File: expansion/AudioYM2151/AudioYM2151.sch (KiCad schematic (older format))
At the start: 3 parts

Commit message: Added YM2151 amp to seperate sheet
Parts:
- removed U?: SN74AVC8T245PW, Package_SO:TSSOP-24_4.4x7.8mm_P0.65mm, symbol Logic_LevelTranslator:SN74AVC8T245PW
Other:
- moved on the sheet: J?, U?
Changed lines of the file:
@@
 $Descr A3 16535 11693
 encoding utf-8
-Sheet 1 2
+Sheet 1 4
 Title ""
 Date ""
@@
 L CPLD_Xilinx:XC95144XL-TQ100 U?
 U 1 1 60B018A5
-P 8900 4200
-F 0 "U?" H 8900 7081 50  0000 C CNN
-F 1 "XC95144XL-TQ100" H 8900 6990 50  0000 C CNN
-F 2 "Package_QFP:TQFP-100_14x14mm_P0.5mm" H 8900 4200 50  0001 C CNN
-F 3 "https://www.xilinx.com/support/documentation/data_sheets/ds056.pdf" H 8900 4200 50  0001 C CNN
-	1    8900 4200
+P 7100 3750
+F 0 "U?" H 7100 6631 50  0000 C CNN
+F 1 "XC95144XL-TQ100" H 7100 6540 50  0000 C CNN
+F 2 "Package_QFP:TQFP-100_14x14mm_P0.5mm" H 7100 3750 50  0001 C CNN
+F 3 "https://www.xilinx.com/support/documentation/data_sheets/ds056.pdf" H 7100 3750 50  0001 C CNN
+	1    7100 3750
 	1    0    0    -1
 $EndComp
@@
 L Ddraig:D68K_64PIN_BOARD J?
 U 1 1 60B07460
-P 2950 4000
-F 0 "J?" H 2925 6065 50  0000 C CNN
-F 1 "D68K_64PIN_BOARD" H 2925 5974 50  0000 C CNN
-F 2 "Ddraig:DIN41612_C_2x32_Male_Horizontal_THT" H 2800 2750 50  0001 C CNN
-F 3 "" H 2800 2750 50  0001 C CNN
-	1    2950 4000
+P 2900 3500
+F 0 "J?" H 2875 5565 50  0000 C CNN
+F 1 "D68K_64PIN_BOARD" H 2875 5474 50  0000 C CNN
+F 2 "Ddraig:DIN41612_C_2x32_Male_Horizontal_THT" H 2750 2250 50  0001 C CNN
+F 3 "" H 2750 2250 50  0001 C CNN
+	1    2900 3500
 	1    0    0    -1
 $EndComp
 $Sheet
-S 11900 3250 1850 2000
+S 10300 5700 1850 1550
 U 60B0BE0A
-F0 "Audio" 50
-F1 "Audio.sch" 50
+F0 "YM2151" 50
+F1 "YM2151.sch" 50
+F2 "A1" I L 10300 6000 50
+F3 "~CS_YM" I L 10300 6100 50
+F4 "~RD_YM" I L 10300 6200 50
+F5 "~WR_YM" I L 10300 6300 50
+F6 "~RESET" I L 10300 6400 50
+F7 "~IRQ" I L 10300 6500 50
+F8 "SPI_DI" I L 10300 6650 50
+F9 "SPI_CLK" I L 10300 6750 50
+F10 "SPI_YMCLK" I L 10300 6850 50
+F11 "YM_AUDIO_L" O R 12150 6050 50
+F12 "YM_AUDIO_R" O R 12150 6150 50
 $EndSheet
-$Comp
-L Logic_LevelTranslator:SN74AVC8T245PW U?
-U 1 1 60B052FD
-P 6350 3950
-F 0 "U?" H 6350 3161 50  0000 C CNN
-F 1 "SN74AVC8T245PW" H 6350 3070 50  0000 C CNN
-F 2 "Package_SO:TSSOP-24_4.4x7.8mm_P0.65mm" H 7250 3300 50  0001 C CNN
-F 3 "https://www.ti.com/lit/ds/symlink/sn74avc8t245.pdf" H 6300 3700 50  0001 C CNN
-	1    6350 3950
-	1    0    0    -1
-$EndComp
+$Sheet
+S 13350 4300 1350 1250
+U 60CBD7B5
+F0 "Amplifier" 50
+F1 "Amplifier.sch" 50
+$EndSheet
+$Sheet
+S 10450 2700 1800 1400
+U 60D530A5
+F0 "ADPCM" 50
+F1 "ADPCM.sch" 50
+$EndSheet
 $EndSCHEMATC

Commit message: More work on YM2151
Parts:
- removed U?: XC95144XL-TQ100, Package_QFP:TQFP-100_14x14mm_P0.5mm, symbol CPLD_Xilinx:XC95144XL-TQ100
- added C? (x3): 100nF, symbol Device:C
- added D?: LED, symbol Device:LED
- added R?: 10K, symbol Device:R
- added R?: 150R, symbol Device:R
- added U?: XC95144XL-TQ100, Package_QFP:TQFP-100_14x14mm_P0.5mm, symbol CPLD_Xilinx:XC95144XL-TQ100
- added U? (x5): 74LS125, symbol 74xx:74LS125
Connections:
- net +5V: now reaches J?.A1 (+5V)
- net +5V: now also J?.A24 (+5V), J?.C1 (+5V), C?.1, C?.1, C?.1, U?.10, U?.12, U?.13, U?.14 (VCC), U?.9
- net D14: now reaches J?.A10 (D14)
- net D14: now also U?.79 (P79)
- net GND: now reaches J?.A11 (GND)
- net GND: now also J?.A2 (GND), J?.A32 (GND), J?.C11 (GND), J?.C24 (GND), J?.C29 (~PRD), J?.C32 (GND), C?.2, C?.2, C?.2, D?.1 (K), R?.2, U?.100 (GND), U?.2, U?.21 (GND), U?.31 (GND), U?.44 (GND), U?.5, U?.62 (GND), U?.69 (GND), U?.7 (GND), U?.75 (GND), U?.84 (GND)
- net A1: now reaches J?.A12 (A1)
- net A1: now also U?.11 (P11)
- net A3: now reaches J?.A13 (A3)
- net A3: now also U?.13 (P13)
- net A5: now reaches J?.A14 (A5)
- net A5: now also U?.15 (P15)
- net A7: now reaches J?.A15 (A7)
- net A7: now also U?.17 (P17)
- net ~LDS: now reaches J?.A25 (~LDS)
- net R~W: now reaches J?.A26 (R/~W)
- net CS_REG: now reaches J?.A27 (~ID)
- net at J?.A28 (~IRQ): now also U?.3
- net D0: now reaches J?.A3 (D0)
- net D0: now also U?.35 (P35)
- net +12V: now reaches J?.A31 (+12V)
- net +12V: now also J?.C31 (+12V)
- net D2: now reaches J?.A4 (D2)
- net D2: now also U?.37 (P37)
- net D4: now reaches J?.A5 (D4)
- net D4: now also U?.40 (P40)
- net D6: now reaches J?.A6 (D6)
- net D6: now also U?.42 (P42)
- net D8: now reaches J?.A7 (D8)
- net D8: now also U?.46 (P46)
- net D10: now reaches J?.A8 (D10)
- net D10: now also U?.74 (P74)
- net D12: now reaches J?.A9 (D12)
- net D12: now also U?.77 (P77)
- net D15: now reaches J?.C10 (D15)
- net D15: now also U?.80 (P80)
- net A2: now reaches J?.C12 (A2)
- net A2: now also U?.12 (P12)
- net A4: now reaches J?.C13 (A4)
- net A4: now also U?.14 (P14)
- net A6: now reaches J?.C14 (A6)
- net A6: now also U?.16 (P16)
- net SYS_CLK: now reaches J?.C23 (SYS_CLK)
- net SYS_CLK: now also U?.22 (I/O/GCK1)
- net ~UDS: now reaches J?.C25 (~UDS)
- net ~RESET: now reaches J?.C26 (~RESET)
- net CS_DATA: now reaches J?.C27 (~CS)
- net at J?.C28 (~ACK): now also U?.6
- net D1: now reaches J?.C3 (D1)
- net D1: now also U?.36 (P36)
- net +3V3: now reaches J?.C30 (+3.3V)
- net +3V3: now also U?.26 (VCCIO), U?.38 (VCCIO), U?.5 (VCCINT), U?.51 (VCCIO), U?.57 (VCCINT), U?.88 (VCCIO), U?.98 (VCCINT)
- net D3: now reaches J?.C4 (D3)
- net D3: now also U?.39 (P39)
- net D5: now reaches J?.C5 (D5)
- net D5: now also U?.41 (P41)
- net D7: now reaches J?.C6 (D7)
- net D7: now also U?.43 (P43)
- net D9: now reaches J?.C7 (D9)
- net D9: now also U?.49 (P49)
- net D11: now reaches J?.C8 (D11)
- net D11: now also U?.76 (P76)
- net D13: now reaches J?.C9 (D13)
- net D13: now also U?.78 (P78)
- new net: D?.2 (A), R?.2
- new net LED: R?.1
- new net MCK: U?.23 (I/O/GCK2)
- new net SPI_DI: R?.1, U?.97 (P97)
- new net ~DTACK: U?.4
- new net ~IRQ: U?.1
- no-connect marks 0 -> 19
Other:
- moved on the sheet: J?

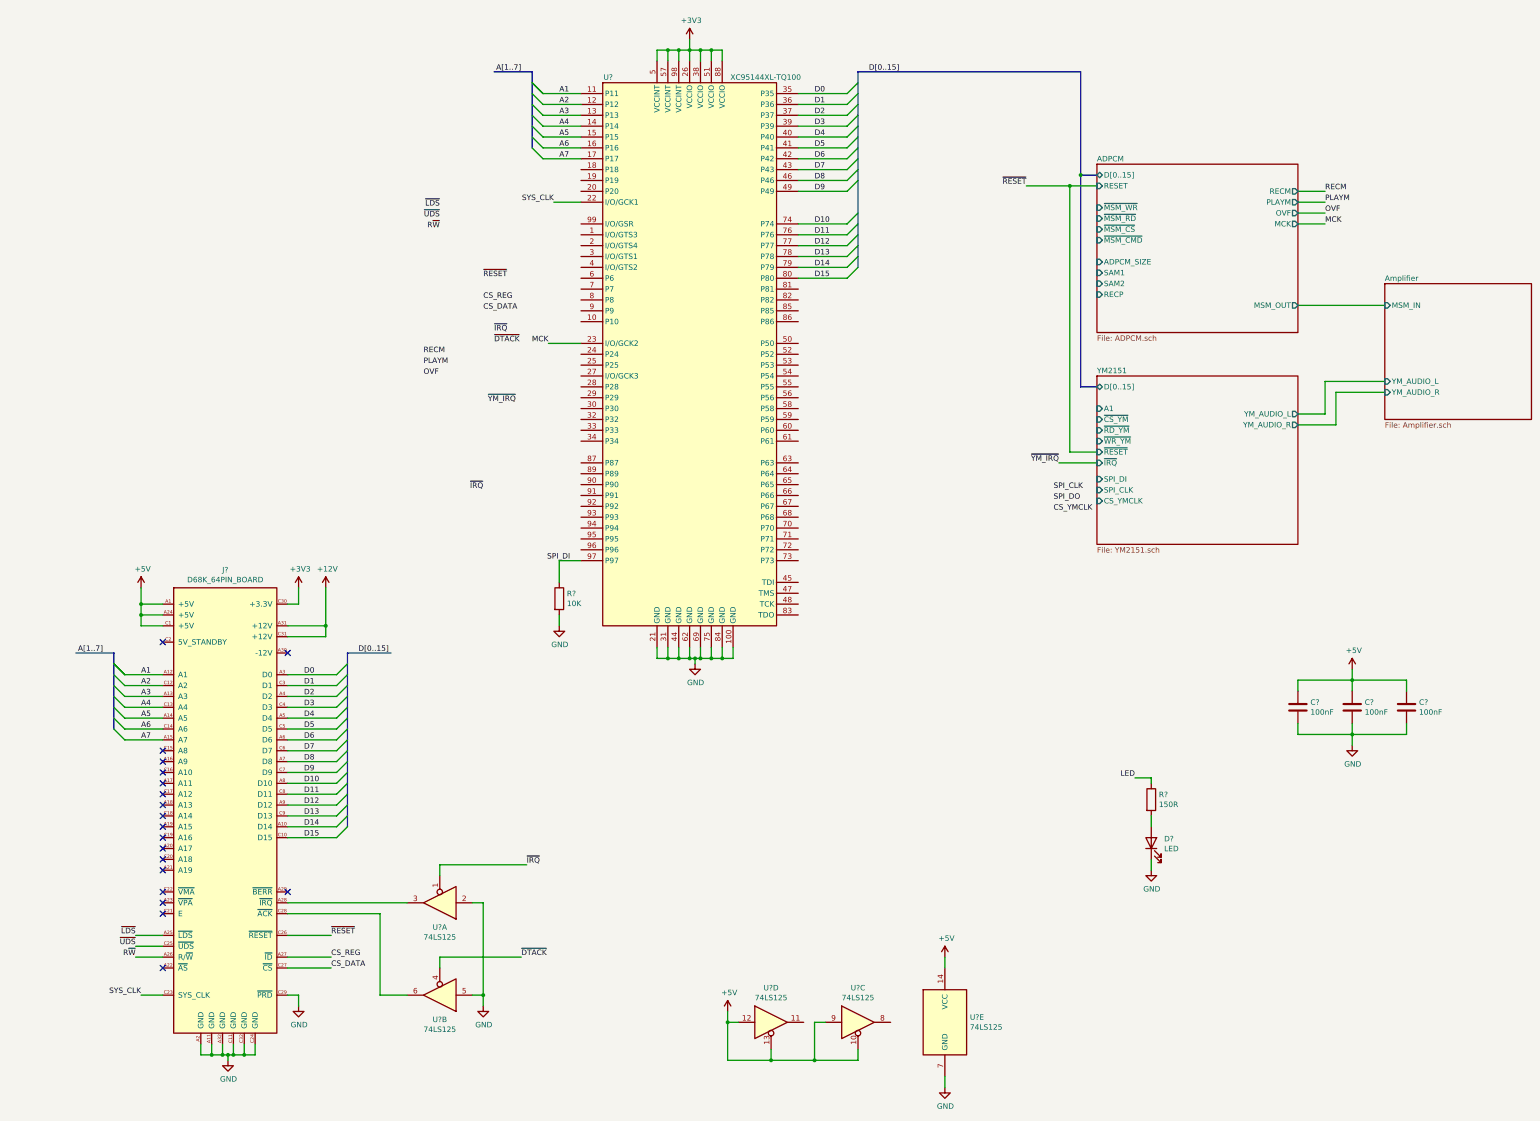
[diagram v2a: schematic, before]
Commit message: Started YM2151 board layout
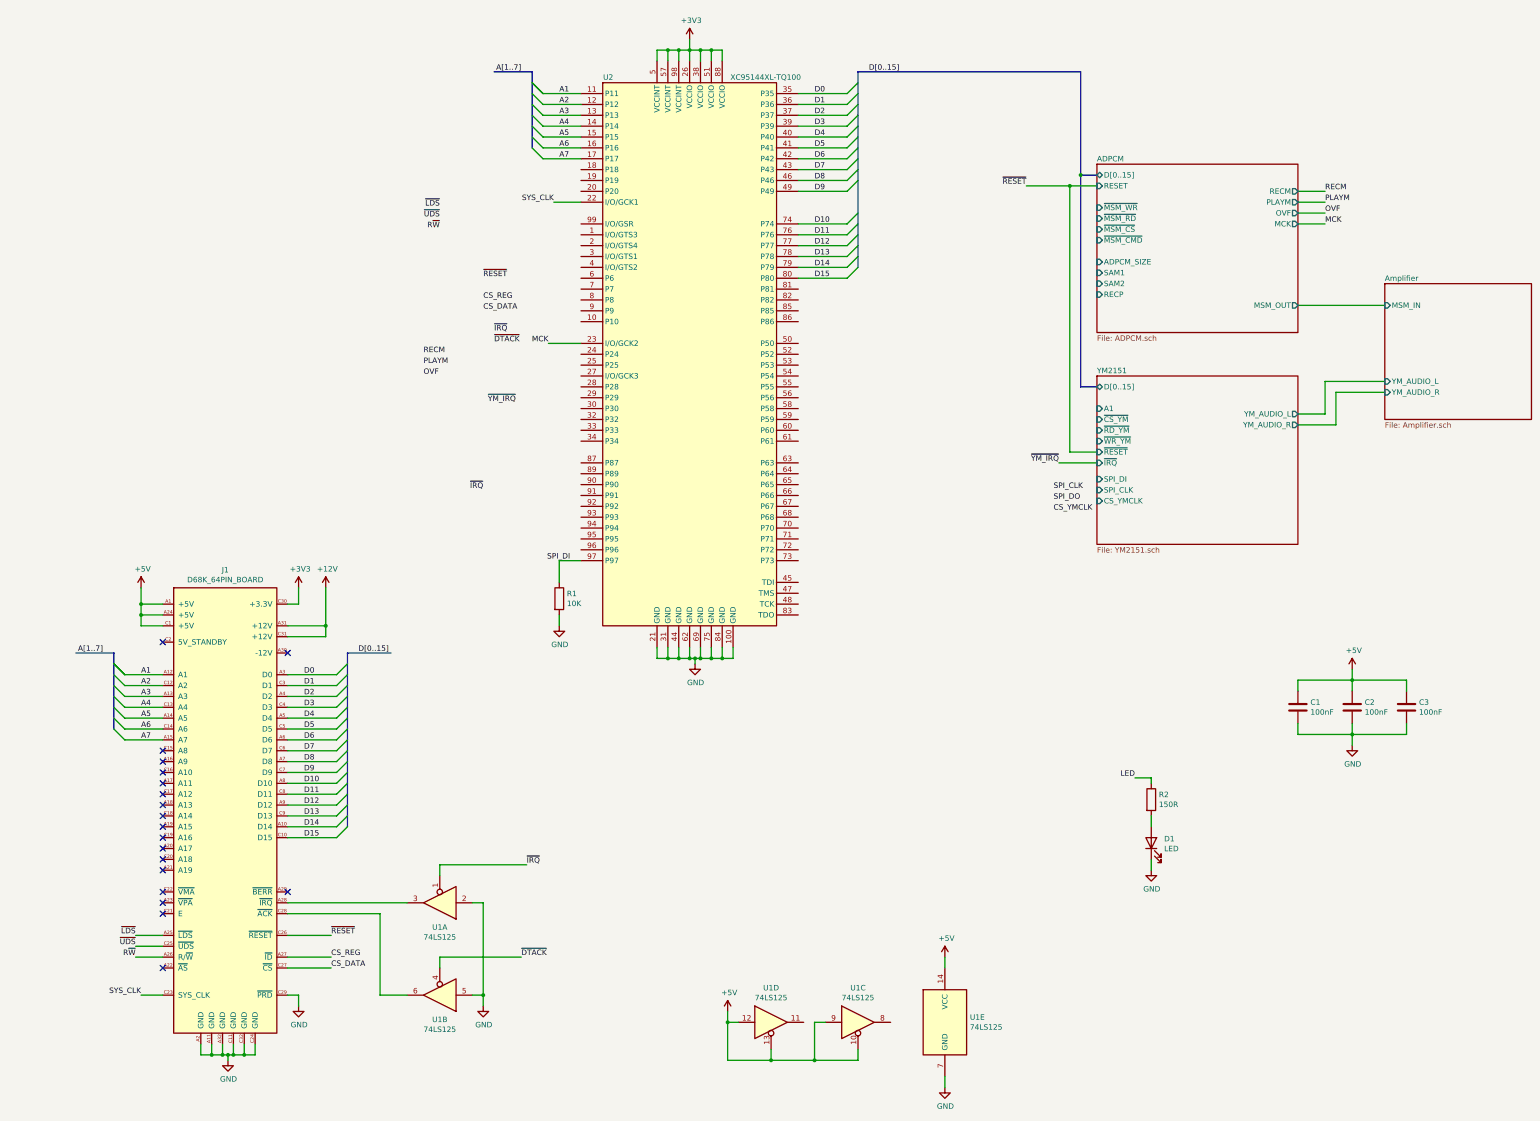
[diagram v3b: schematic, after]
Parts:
- C1, C2, C3: renamed from C?; footprint (none) -> Capacitor_THT:C_Disc_D5.0mm_W2.5mm_P2.50mm
- D1: renamed from D?; footprint (none) -> LED_THT:LED_D5.0mm
- R1, R2: renamed from R?; footprint (none) -> Resistor_THT:R_Axial_DIN0207_L6.3mm_D2.5mm_P10.16mm_Horizontal
- U1: renamed from U?; footprint (none) -> Package_DIP:DIP-14_W7.62mm_Socket
- gave numbers to parts that had none: 2
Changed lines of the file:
@@
 $EndDescr
 $Comp
-L Ddraig:D68K_64PIN_BOARD J?
+L Ddraig:D68K_64PIN_BOARD J1
 U 1 1 60B07460
 P 2850 8050
-F 0 "J?" H 2825 10115 50  0000 C CNN
+F 0 "J1" H 2825 10115 50  0000 C CNN
 F 1 "D68K_64PIN_BOARD" H 2825 10024 50  0000 C CNN
 F 2 "Ddraig:DIN41612_C_2x32_Male_Horizontal_THT" H 2700 6800 50  0001 C CNN
@@
 $EndSheet
 $Comp
-L CPLD_Xilinx:XC95144XL-TQ100 U?
+L CPLD_Xilinx:XC95144XL-TQ100 U2
 U 1 1 60CC8E00
 P 7100 4000
-F 0 "U?" H 6350 6550 50  0000 C CNN
+F 0 "U2" H 6350 6550 50  0000 C CNN
 F 1 "XC95144XL-TQ100" H 7800 6550 50  0000 C CNN
 F 2 "Package_QFP:TQFP-100_14x14mm_P0.5mm" H 7100 4000 50  0001 C CNN
@@
 NoConn ~ 3400 6750
 $Comp
-L power:+5V #PWR?
+L power:+5V #PWR0101
 U 1 1 60CD3C32
 P 2050 6150
-F 0 "#PWR?" H 2050 6000 50  0001 C CNN
+F 0 "#PWR0101" H 2050 6000 50  0001 C CNN
 F 1 "+5V" H 2065 6323 50  0000 C CNN
 F 2 "" H 2050 6150 50  0001 C CNN
@@
 $EndComp
 $Comp
-L power:+12V #PWR?
+L power:+12V #PWR0102
 U 1 1 60CD44DB
 P 3750 6150
-F 0 "#PWR?" H 3750 6000 50  0001 C CNN
+F 0 "#PWR0102" H 3750 6000 50  0001 C CNN
 F 1 "+12V" H 3765 6323 50  0000 C CNN
 F 2 "" H 3750 6150 50  0001 C CNN
@@
 NoConn ~ 3400 8950
 $Comp
-L power:GND #PWR?
+L power:GND #PWR0103
 U 1 1 60CE1A9B
 P 2850 10500
-F 0 "#PWR?" H 2850 10250 50  0001 C CNN
+F 0 "#PWR0103" H 2850 10250 50  0001 C CNN
 F 1 "GND" H 2855 10327 50  0000 C CNN
 F 2 "" H 2850 10500 50  0001 C CNN
@@
 $EndComp
 $Comp
-L power:GND #PWR?
+L power:GND #PWR0104
 U 1 1 60CE1DAE
 P 3500 10000
-F 0 "#PWR?" H 3500 9750 50  0001 C CNN
+F 0 "#PWR0104" H 3500 9750 50  0001 C CNN
 F 1 "GND" H 3505 9827 50  0000 C CNN
 F 2 "" H 3500 10000 50  0001 C CNN
@@
 	6100 2600 5850 2600
 $Comp
-L power:GND #PWR?
+L power:GND #PWR0105
 U 1 1 60CF6212
 P 7150 6850
-F 0 "#PWR?" H 7150 6600 50  0001 C CNN
+F 0 "#PWR0105" H 7150 6600 50  0001 C CNN
 F 1 "GND" H 7155 6677 50  0000 C CNN
 F 2 "" H 7150 6850 50  0001 C CNN
@@
 $EndComp
 $Comp
-L power:+3V3 #PWR?
+L power:+3V3 #PWR0106
 U 1 1 60CFD09B
 P 3500 6150
-F 0 "#PWR?" H 3500 6000 50  0001 C CNN
+F 0 "#PWR0106" H 3500 6000 50  0001 C CNN
 F 1 "+3V3" H 3515 6323 50  0000 C CNN
 F 2 "" H 3500 6150 50  0001 C CNN
@@
 	3500 6300 3500 6150
 $Comp
-L power:+3V3 #PWR?
+L power:+3V3 #PWR0107
 U 1 1 60CFFBD2
 P 7100 1100
-F 0 "#PWR?" H 7100 950 50  0001 C CNN
+F 0 "#PWR0107" H 7100 950 50  0001 C CNN
 F 1 "+3V3" H 7115 1273 50  0000 C CNN
 F 2 "" H 7100 1100 50  0001 C CNN
@@
 	7150 6800 7200 6800
 $Comp
-L 74xx:74LS125 U?
+L 74xx:74LS125 U1
 U 1 1 60F01C16
 P 4800 9050
-F 0 "U?" H 4800 9275 50  0000 C CNN
+F 0 "U1" H 4800 9275 50  0000 C CNN
 F 1 "74LS125" H 4800 9366 50  0000 C CNN
-F 2 "" H 4800 9050 50  0001 C CNN
+F 2 "Package_DIP:DIP-14_W7.62mm_Socket" H 4800 9050 50  0001 C CNN
 F 3 "http://www.ti.com/lit/gpn/sn74LS125" H 4800 9050 50  0001 C CNN
 	1    4800 9050
@@
 $EndComp
 $Comp
-L 74xx:74LS125 U?
+L 74xx:74LS125 U1
 U 2 1 60F033E0
 P 4800 9900
-F 0 "U?" H 4800 10125 50  0000 C CNN
+F 0 "U1" H 4800 10125 50  0000 C CNN
 F 1 "74LS125" H 4800 10216 50  0000 C CNN
-F 2 "" H 4800 9900 50  0001 C CNN
+F 2 "Package_DIP:DIP-14_W7.62mm_Socket" H 4800 9900 50  0001 C CNN
 F 3 "http://www.ti.com/lit/gpn/sn74LS125" H 4800 9900 50  0001 C CNN
 	2    4800 9900
@@
 $EndComp
 $Comp
-L 74xx:74LS125 U?
+L 74xx:74LS125 U1
 U 3 1 60F0459B
 P 8650 10150
-F 0 "U?" H 8650 10467 50  0000 C CNN
+F 0 "U1" H 8650 10467 50  0000 C CNN
 F 1 "74LS125" H 8650 10376 50  0000 C CNN
-F 2 "" H 8650 10150 50  0001 C CNN
+F 2 "Package_DIP:DIP-14_W7.62mm_Socket" H 8650 10150 50  0001 C CNN
 F 3 "http://www.ti.com/lit/gpn/sn74LS125" H 8650 10150 50  0001 C CNN
 	3    8650 10150
@@
 $EndComp
 $Comp
-L 74xx:74LS125 U?
+L 74xx:74LS125 U1
 U 4 1 60F05376
 P 7850 10150
-F 0 "U?" H 7850 10467 50  0000 C CNN
+F 0 "U1" H 7850 10467 50  0000 C CNN
 F 1 "74LS125" H 7850 10376 50  0000 C CNN
-F 2 "" H 7850 10150 50  0001 C CNN
+F 2 "Package_DIP:DIP-14_W7.62mm_Socket" H 7850 10150 50  0001 C CNN
 F 3 "http://www.ti.com/lit/gpn/sn74LS125" H 7850 10150 50  0001 C CNN
 	4    7850 10150
@@
 $EndComp
 $Comp
-L 74xx:74LS125 U?
+L 74xx:74LS125 U1
 U 5 1 60F0634B
 P 9450 10150
-F 0 "U?" H 9680 10196 50  0000 L CNN
+F 0 "U1" H 9680 10196 50  0000 L CNN
 F 1 "74LS125" H 9680 10105 50  0000 L CNN
-F 2 "" H 9450 10150 50  0001 C CNN
+F 2 "Package_DIP:DIP-14_W7.62mm_Socket" H 9450 10150 50  0001 C CNN
 F 3 "http://www.ti.com/lit/gpn/sn74LS125" H 9450 10150 50  0001 C CNN
 	5    9450 10150
@@
 	3400 9050 4500 9050
 $Comp
-L power:GND #PWR?
+L power:GND #PWR0108
 U 1 1 60F2C3F3
 P 5200 10000
-F 0 "#PWR?" H 5200 9750 50  0001 C CNN
+F 0 "#PWR0108" H 5200 9750 50  0001 C CNN
 F 1 "GND" H 5205 9827 50  0000 C CNN
 F 2 "" H 5200 10000 50  0001 C CNN
@@
 	4800 8700 5600 8700
 $Comp
-L power:GND #PWR?
+L power:GND #PWR0109
 U 1 1 60F41EEB
 P 9450 10750
-F 0 "#PWR?" H 9450 10500 50  0001 C CNN
+F 0 "#PWR0109" H 9450 10500 50  0001 C CNN
 F 1 "GND" H 9455 10577 50  0000 C CNN
 F 2 "" H 9450 10750 50  0001 C CNN
@@
 $EndComp
 $Comp
-L power:+5V #PWR?
+L power:+5V #PWR0110
 U 1 1 60F4243B
 P 9450 9550
-F 0 "#PWR?" H 9450 9400 50  0001 C CNN
+F 0 "#PWR0110" H 9450 9400 50  0001 C CNN
 F 1 "+5V" H 9465 9723 50  0000 C CNN
 F 2 "" H 9450 9550 50  0001 C CNN
@@
 	9450 10650 9450 10750
 $Comp
-L power:+5V #PWR?
+L power:+5V #PWR0111
 U 1 1 60F4D90B
 P 7450 10050
-F 0 "#PWR?" H 7450 9900 50  0001 C CNN
+F 0 "#PWR0111" H 7450 9900 50  0001 C CNN
 F 1 "+5V" H 7465 10223 50  0000 C CNN
 F 2 "" H 7450 10050 50  0001 C CNN
@@
 CS_YMCLK
 $Comp
-L Device:R R?
+L Device:R R1
 U 1 1 60FF10BA
 P 5900 6250
-F 0 "R?" H 5970 6296 50  0000 L CNN
+F 0 "R1" H 5970 6296 50  0000 L CNN
 F 1 "10K" H 5970 6205 50  0000 L CNN
-F 2 "" V 5830 6250 50  0001 C CNN
+F 2 "Resistor_THT:R_Axial_DIN0207_L6.3mm_D2.5mm_P10.16mm_Horizontal" V 5830 6250 50  0001 C CNN
 F 3 "~" H 5900 6250 50  0001 C CNN
 	1    5900 6250
@@
 $EndComp
 $Comp
-L power:GND #PWR?
+L power:GND #PWR0112
 U 1 1 60FF1314
 P 5900 6500
-F 0 "#PWR?" H 5900 6250 50  0001 C CNN
+F 0 "#PWR0112" H 5900 6250 50  0001 C CNN
 F 1 "GND" H 5905 6327 50  0000 C CNN
 F 2 "" H 5900 6500 50  0001 C CNN
@@
 SPI_DI
 $Comp
-L Device:C C?
+L Device:C C3
 U 1 1 610B08A2
 P 13700 7250
-F 0 "C?" H 13815 7296 50  0000 L CNN
+F 0 "C3" H 13815 7296 50  0000 L CNN
 F 1 "100nF" H 13815 7205 50  0000 L CNN
-F 2 "" H 13738 7100 50  0001 C CNN
+F 2 "Capacitor_THT:C_Disc_D5.0mm_W2.5mm_P2.50mm" H 13738 7100 50  0001 C CNN
 F 3 "~" H 13700 7250 50  0001 C CNN
 	1    13700 7250
@@
 $EndComp
 $Comp
-L Device:C C?
+L Device:C C2
 U 1 1 610B08A8
 P 13200 7250
-F 0 "C?" H 13315 7296 50  0000 L CNN
+F 0 "C2" H 13315 7296 50  0000 L CNN
 F 1 "100nF" H 13315 7205 50  0000 L CNN
-F 2 "" H 13238 7100 50  0001 C CNN
+F 2 "Capacitor_THT:C_Disc_D5.0mm_W2.5mm_P2.50mm" H 13238 7100 50  0001 C CNN
 F 3 "~" H 13200 7250 50  0001 C CNN
 	1    13200 7250
@@
 $EndComp
 $Comp
-L Device:C C?
+L Device:C C1
 U 1 1 610B08AE
 P 12700 7250
-F 0 "C?" H 12815 7296 50  0000 L CNN
+F 0 "C1" H 12815 7296 50  0000 L CNN
 F 1 "100nF" H 12815 7205 50  0000 L CNN
-F 2 "" H 12738 7100 50  0001 C CNN
+F 2 "Capacitor_THT:C_Disc_D5.0mm_W2.5mm_P2.50mm" H 12738 7100 50  0001 C CNN
 F 3 "~" H 12700 7250 50  0001 C CNN
 	1    12700 7250
@@
 P 13200 7600
 AR Path="/60D530A5/610B08B4" Ref="#PWR?"  Part="1"
-AR Path="/610B08B4" Ref="#PWR?"  Part="1"
-F 0 "#PWR?" H 13200 7350 50  0001 C CNN
+AR Path="/610B08B4" Ref="#PWR0113"  Part="1"
+F 0 "#PWR0113" H 13200 7350 50  0001 C CNN
 F 1 "GND" H 13205 7427 50  0000 C CNN
 F 2 "" H 13200 7600 50  0001 C CNN
@@
 $EndComp
 $Comp
-L power:+5V #PWR?
+L power:+5V #PWR0114
 U 1 1 610B08BA
 P 13200 6900
-F 0 "#PWR?" H 13200 6750 50  0001 C CNN
+F 0 "#PWR0114" H 13200 6750 50  0001 C CNN
 F 1 "+5V" H 13215 7073 50  0000 C CNN
 F 2 "" H 13200 6900 50  0001 C CNN
@@
 	13200 7500 13200 7600
 $Comp
-L Device:R R?
+L Device:R R2
 U 1 1 610B9469
 P 11350 8100
-F 0 "R?" H 11420 8146 50  0000 L CNN
+F 0 "R2" H 11420 8146 50  0000 L CNN
 F 1 "150R" H 11420 8055 50  0000 L CNN
-F 2 "" V 11280 8100 50  0001 C CNN
+F 2 "Resistor_THT:R_Axial_DIN0207_L6.3mm_D2.5mm_P10.16mm_Horizontal" V 11280 8100 50  0001 C CNN
 F 3 "~" H 11350 8100 50  0001 C CNN
 	1    11350 8100
@@
 $EndComp
 $Comp
-L Device:LED D?
+L Device:LED D1
 U 1 1 610B9D98
 P 11350 8500
-F 0 "D?" V 11389 8382 50  0000 R CNN
+F 0 "D1" V 11389 8382 50  0000 R CNN
 F 1 "LED" V 11298 8382 50  0000 R CNN
-F 2 "" H 11350 8500 50  0001 C CNN
+F 2 "LED_THT:LED_D5.0mm" H 11350 8500 50  0001 C CNN
 F 3 "~" H 11350 8500 50  0001 C CNN
 	1    11350 8500
@@
 P 11350 8750
 AR Path="/60D530A5/610C26E3" Ref="#PWR?"  Part="1"
-AR Path="/610C26E3" Ref="#PWR?"  Part="1"
-F 0 "#PWR?" H 11350 8500 50  0001 C CNN
+AR Path="/610C26E3" Ref="#PWR0115"  Part="1"
+F 0 "#PWR0115" H 11350 8500 50  0001 C CNN
 F 1 "GND" H 11355 8577 50  0000 C CNN
 F 2 "" H 11350 8750 50  0001 C CNN
